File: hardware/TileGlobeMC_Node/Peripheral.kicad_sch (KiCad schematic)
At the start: 0 parts

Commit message: PCB progress
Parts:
- added C27: 4.7u, Capacitor_SMD:C_0603_1608Metric, symbol Device:C_Small
- added C28, C29, C30, C31, C32, C33, C34, C35: 100n, Capacitor_SMD:C_0603_1608Metric, symbol Device:C_Small
- added D3: 3V, Diode_SMD:D_SOD-323_HandSoldering, symbol Device:D_Zener_Small
- added J10: LCD, Connector_FFC-FPC:TE_1-1734839-2_1x12-1MP_P0.5mm_Horizontal, symbol Connector_Generic_MountingPin:Conn_01x12_MountingPin
- added JP3: BL_P1_1, Jumper:SolderJumper-2_P1.3mm_Open_TrianglePad1.0x1.5mm, symbol Jumper:SolderJumper_2_Open
- added JP4: BL_P1_2, Jumper:SolderJumper-2_P1.3mm_Open_TrianglePad1.0x1.5mm, symbol Jumper:SolderJumper_2_Open
- added JP5: BL_P1_3, Jumper:SolderJumper-2_P1.3mm_Open_TrianglePad1.0x1.5mm, symbol Jumper:SolderJumper_2_Open
- added R31, R42, R43, R44, R45, R46, R47: 100k, Capacitor_SMD:C_0603_1608Metric, symbol Device:R_Small
- added R35, R38, R39, R40, R41: 10k, Capacitor_SMD:C_0603_1608Metric, symbol Device:R_Small
- added SW1, SW2, SW3, SW4, SW5: Left, Button_Switch_SMD:SW_SPST_PTS647_Sx38, symbol Switch:SW_Push
- added U8: LSM6DS3, Package_LGA:LGA-14_3x2.5mm_P0.5mm_LayoutBorder3x4y, symbol Sensor_Motion:LSM6DS3
- added U9: AW9523B, Package_DFN_QFN:QFN-24-1EP_4x4mm_P0.5mm_EP2.7x2.7mm, symbol Interface_Expansion:AW9523B
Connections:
- new net: R38.1, SW2.1
- new net: R41.1, SW5.1
- new net: R39.1, SW3.1
- new net: JP3.1 (A), U9.2 (P1_1)
- new net: R40.1, SW4.1
- new net: JP4.1 (A), U9.3 (P1_2)
- new net: JP5.1 (A), U9.4 (P1_3)
- new net +3V3: C27.1, C28.1, C29.1, C35.1, J10.3 (Pin_3), J10.4 (Pin_4), R46.1, R47.1, SW2.2, SW3.2, SW4.2, SW5.2, U8.12 (CS), U8.5 (VDDIO), U8.8 (VDD), U9.18 (AD0), U9.21 (VCC), U9.23 (~{RST})
- new net BTN_BOTTOM: C32.1, R39.2, R42.1, U9.11 (P0_5)
- new net BTN_CENTER: C30.1, D3.1 (K), R35.2, R45.1
- new net BTN_CENTER_VBUS: R35.1, SW1.1
- new net BTN_LEFT: C31.1, R31.1, R38.2, U9.10 (P0_4)
- new net BTN_RIGHT: C33.1, R40.2, R43.1, U9.12 (P0_6)
- new net BTN_TOP: C34.1, R41.2, R44.1, U9.13 (P0_7)
- new net GND_PERI: C27.2, C28.2, C29.2, C30.2, C31.2, C32.2, C33.2, C34.2, C35.2, D3.2 (A), J10.1 (Pin_1), J10.12 (Pin_12), J10.5 (Pin_5), J10.6 (Pin_6), J10.MP (MountPin), R31.2, R42.2, R43.2, R44.2, R45.2, U8.1 (SDO/SA0), U8.2 (SDX), U8.3 (SCX), U8.6 (GND), U8.7 (GND), U9.24 (AD1), U9.25 (GND), U9.9 (GND)
- new net I2C_SCL: U8.13 (SCL), U9.19 (SCL)
- new net I2C_SDA: U8.14 (SDA), U9.20 (SDA)
- new net IMU_INT1: R46.2, U8.4 (INT1), U9.5 (P0_0)
- new net IMU_INT2: R47.2, U8.9 (INT2), U9.6 (P0_1)
- new net LCD_BL: J10.2 (Pin_2), JP3.2 (B), JP4.2 (B), JP5.2 (B), U9.1 (P1_0)
- new net LCD_CS: J10.8 (Pin_8)
- new net LCD_DC: J10.7 (Pin_7)
- new net LCD_MOSI: J10.10 (Pin_10)
- new net LCD_RST: J10.11 (Pin_11), U9.17 (P1_7)
- new net LCD_SCK: J10.9 (Pin_9)
- new net PERI_INT: U9.22 (~{INT})
- new net VBUS: SW1.2
- no-connect marks 0 -> 5
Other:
- note added: "Buttons"
- note added: "I2C Addr: 0x59"
- note added: "I2C Addr: 0x6A"
- note added: "I2C IO Expander & LCD BL Driver"
- note added: "IMU"
- note added: "LCD"

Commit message: PCB progress
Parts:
- added H5, H6, H7, H8: MountingHole, MountingHole:MountingHole_2.2mm_M2, symbol Mechanical:MountingHole
- added J11: USB_C, Connector_USB:USB_C_Receptacle_GCT_USB4105-xx-A_16P_TopMnt_Horizontal, symbol Connector:USB_C_Receptacle_USB2.0_16P
- added R32, R33: 5.1k, Resistor_SMD:R_0603_1608Metric, symbol Device:R_Small
- added R36, R37: 10k, Resistor_SMD:R_0603_1608Metric, symbol Device:R_Small
- D3: footprint Diode_SMD:D_SOD-323_HandSoldering -> Diode_SMD:D_SOD-523
- R31, R35, R38, R39, R40, R41, R42, R43, R44, R45, R46, R47: footprint Capacitor_SMD:C_0603_1608Metric -> Resistor_SMD:R_0603_1608Metric
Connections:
- net +3V3: now also R36.2, R37.2
- net GND_PERI: now also J11.A1 (GND), J11.A12 (GND), J11.B1 (GND), J11.B12 (GND), J11.S1 (SHIELD), R32.1, R33.1
- net I2C_SCL: now also R36.1
- net I2C_SDA: now also R37.1
- new net: J11.A5 (CC1), R33.2
- new net: J11.B5 (CC2), R32.2
- new net USB_D+: J11.A6 (D+), J11.B6 (D+)
- new net USB_D-: J11.A7 (D-), J11.B7 (D-)
- new net VIN: J11.A4 (VBUS), J11.A9 (VBUS), J11.B4 (VBUS), J11.B9 (VBUS)
- no-connect marks 5 -> 7
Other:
- note added: "USB-C"

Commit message: PCB done
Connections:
- net +3V3: now also J10.10 (Pin_10), J10.9 (Pin_9); no longer J10.3 (Pin_3), J10.4 (Pin_4)
- net BTN_BOTTOM: now also U9.10 (P0_4); no longer U9.11 (P0_5)
- net BTN_LEFT: now also U9.12 (P0_6); no longer U9.10 (P0_4)
- net BTN_RIGHT: now also U9.11 (P0_5); no longer U9.12 (P0_6)
- net GND_PERI: now also J10.7 (Pin_7), J10.8 (Pin_8); no longer J10.5 (Pin_5), J10.6 (Pin_6)
- net IMU_INT1: now also U9.7 (P0_2); no longer U9.5 (P0_0)
- net IMU_INT2: now also U9.8 (P0_3); no longer U9.6 (P0_1)
- net LCD_BL: now also J10.11 (Pin_11); no longer J10.2 (Pin_2)
- net LCD_CS: now also J10.5 (Pin_5); no longer J10.8 (Pin_8)
- net LCD_DC: now also J10.6 (Pin_6); no longer J10.7 (Pin_7)
- net LCD_MOSI: now also J10.3 (Pin_3); no longer J10.10 (Pin_10)
- net LCD_RST: now also J10.2 (Pin_2), U9.14 (P1_4); no longer J10.11 (Pin_11), U9.17 (P1_7)
- net LCD_SCK: now also J10.4 (Pin_4); no longer J10.9 (Pin_9)
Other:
- moved on the sheet: J10
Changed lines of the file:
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@@
 	)
 	(no_connect
-		(at 143.51 134.62)
+		(at 143.51 129.54)
 	)
 	(no_connect
-		(at 143.51 132.08)
+		(at 143.51 127)
 	)
 	(no_connect
@@
 	)
 	(no_connect
-		(at 143.51 160.02)
+		(at 143.51 167.64)
 	)
 	(no_connect
@@
 			(table_cell ""
 				(exclude_from_sim no)
-				(at 167.64 146.05 0)
+				(at 162.56 146.05 0)
 				(size 8.89 2.54)
 				(margins 0.9525 0.9525 0.9525 0.9525)
@@
 			(table_cell "1"
 				(exclude_from_sim no)
-				(at 167.64 148.59 0)
+				(at 162.56 148.59 0)
 				(size 8.89 2.54)
 				(margins 0.9525 0.9525 0.9525 0.9525)
@@
 			(table_cell "1"
 				(exclude_from_sim no)
-				(at 167.64 151.13 0)
+				(at 162.56 151.13 0)
 				(size 8.89 2.54)
 				(margins 0.9525 0.9525 0.9525 0.9525)
@@
 			(table_cell "1"
 				(exclude_from_sim no)
-				(at 167.64 153.67 0)
+				(at 162.56 153.67 0)
 				(size 8.89 2.54)
 				(margins 0.9525 0.9525 0.9525 0.9525)
@@
 			(table_cell "1"
 				(exclude_from_sim no)
-				(at 167.64 156.21 0)
+				(at 162.56 156.21 0)
 				(size 8.89 2.54)
 				(margins 0.9525 0.9525 0.9525 0.9525)
@@
 			(table_cell "0"
 				(exclude_from_sim no)
-				(at 167.64 158.75 0)
+				(at 162.56 158.75 0)
 				(size 8.89 2.54)
 				(margins 0.9525 0.9525 0.9525 0.9525)
@@
 			(table_cell "0"
 				(exclude_from_sim no)
-				(at 167.64 161.29 0)
+				(at 162.56 161.29 0)
 				(size 8.89 2.54)
 				(margins 0.9525 0.9525 0.9525 0.9525)
@@
 			(table_cell "0"
 				(exclude_from_sim no)
-				(at 167.64 163.83 0)
+				(at 162.56 163.83 0)
 				(size 8.89 2.54)
 				(margins 0.9525 0.9525 0.9525 0.9525)
@@
 			(table_cell "0"
 				(exclude_from_sim no)
-				(at 167.64 166.37 0)
+				(at 162.56 166.37 0)
 				(size 8.89 2.54)
 				(margins 0.9525 0.9525 0.9525 0.9525)
@@
 			(table_cell "Default"
 				(exclude_from_sim no)
-				(at 167.64 123.19 0)
+				(at 162.56 123.19 0)
 				(size 8.89 2.54)
 				(margins 0.9525 0.9525 0.9525 0.9525)
@@
 			(table_cell "Hi-Z"
 				(exclude_from_sim no)
-				(at 167.64 125.73 0)
+				(at 162.56 125.73 0)
 				(size 8.89 2.54)
 				(margins 0.9525 0.9525 0.9525 0.9525)
@@
 			(table_cell "Hi-Z"
 				(exclude_from_sim no)
-				(at 167.64 128.27 0)
+				(at 162.56 128.27 0)
 				(size 8.89 2.54)
 				(margins 0.9525 0.9525 0.9525 0.9525)
@@
 			(table_cell "Hi-Z"
 				(exclude_from_sim no)
-				(at 167.64 130.81 0)
+				(at 162.56 130.81 0)
 				(size 8.89 2.54)
 				(margins 0.9525 0.9525 0.9525 0.9525)
@@
 			(table_cell "Hi-Z"
 				(exclude_from_sim no)
-				(at 167.64 133.35 0)
+				(at 162.56 133.35 0)
 				(size 8.89 2.54)
 				(margins 0.9525 0.9525 0.9525 0.9525)
@@
 			(table_cell "0"
 				(exclude_from_sim no)
-				(at 167.64 135.89 0)
+				(at 162.56 135.89 0)
 				(size 8.89 2.54)
 				(margins 0.9525 0.9525 0.9525 0.9525)
@@
 			(table_cell "0"
 				(exclude_from_sim no)
-				(at 167.64 138.43 0)
+				(at 162.56 138.43 0)
 				(size 8.89 2.54)
 				(margins 0.9525 0.9525 0.9525 0.9525)
@@
 			(table_cell "0"
 				(exclude_from_sim no)
-				(at 167.64 140.97 0)
+				(at 162.56 140.97 0)
 				(size 8.89 2.54)
 				(margins 0.9525 0.9525 0.9525 0.9525)
@@
 			(table_cell "0"
 				(exclude_from_sim no)
-				(at 167.64 143.51 0)
+				(at 162.56 143.51 0)
 				(size 8.89 2.54)
 				(margins 0.9525 0.9525 0.9525 0.9525)
@@
 	(global_label "LCD_RST"
 		(shape output)
-		(at 143.51 167.64 0)
+		(at 143.51 160.02 0)
 		(fields_autoplaced yes)
 		(effects
@@
 		)
 		(property "Intersheetrefs" "${INTERSHEET_REFS}"
-			(at 154.478 167.64 0)
+			(at 154.478 160.02 0)
 			(effects
 				(font
@@
 	(global_label "BTN_LEFT"
 		(shape input)
-		(at 143.51 137.16 0)
+		(at 143.51 142.24 0)
 		(fields_autoplaced yes)
 		(effects
@@
 		)
 		(property "Intersheetrefs" "${INTERSHEET_REFS}"
-			(at 155.2642 137.16 0)
+			(at 155.2642 142.24 0)
 			(effects
 				(font
@@
 	(global_label "BTN_RIGHT"
 		(shape input)
-		(at 143.51 142.24 0)
+		(at 143.51 139.7 0)
 		(fields_autoplaced yes)
 		(effects
@@
 		)
 		(property "Intersheetrefs" "${INTERSHEET_REFS}"
-			(at 156.4738 142.24 0)
+			(at 156.4738 139.7 0)
 			(effects
 				(font
@@
 	(global_label "BTN_BOTTOM"
 		(shape input)
-		(at 143.51 139.7 0)
+		(at 143.51 137.16 0)
 		(fields_autoplaced yes)
 		(effects
@@
 		)
 		(property "Intersheetrefs" "${INTERSHEET_REFS}"
-			(at 158.3485 139.7 0)
+			(at 158.3485 137.16 0)
 			(effects
 				(font
@@
 	(global_label "IMU_INT2"
 		(shape input)
-		(at 143.51 129.54 0)
+		(at 143.51 134.62 0)
 		(fields_autoplaced yes)
 		(effects
@@
 		)
 		(property "Intersheetrefs" "${INTERSHEET_REFS}"
-			(at 154.9619 129.54 0)
+			(at 154.9619 134.62 0)
 			(effects
 				(font
@@
 	(global_label "IMU_INT1"
 		(shape input)
-		(at 143.51 127 0)
+		(at 143.51 132.08 0)
 		(fields_autoplaced yes)
 		(effects
@@
 		)
 		(property "Intersheetrefs" "${INTERSHEET_REFS}"
-			(at 154.9619 127 0)
+			(at 154.9619 132.08 0)
 			(effects
 				(font
@@
 	(symbol
 		(lib_id "power:GND")
-		(at 154.94 66.04 0)
+		(at 154.94 27.94 90)
 		(unit 1)
 		(exclude_from_sim no)
@@
 		(dnp no)
 		(property "Reference" "#PWR063"
-			(at 154.94 72.39 0)
+			(at 161.29 27.94 0)
 			(effects
 				(font
@@
 		)
 		(property "Value" "GND_PERI"
-			(at 154.94 69.596 0)
+			(at 158.496 27.94 0)
 			(effects
 				(font
@@
 		)
 		(property "Footprint" ""
-			(at 154.94 66.04 0)
+			(at 154.94 27.94 0)
 			(effects
 				(font
@@
 		)
 		(property "Datasheet" ""
-			(at 154.94 66.04 0)
+			(at 154.94 27.94 0)
 			(effects
 				(font
@@
 		)
 		(property "Description" "Power symbol creates a global label with name \"GND\" , ground"
-			(at 154.94 66.04 0)
+			(at 154.94 27.94 0)
 			(effects
 				(font
@@
 	(symbol
 		(lib_id "Connector_Generic_MountingPin:Conn_01x12_MountingPin")
-		(at 154.94 45.72 0)
+		(at 154.94 48.26 0)
+		(mirror x)
 		(unit 1)
 		(exclude_from_sim no)
@@
 		(dnp no)
 		(property "Reference" "J10"
-			(at 164.084 45.974 0)
+			(at 164.084 48.006 0)
 			(effects
 				(font
@@
 		)
 		(property "Value" "LCD"
-			(at 164.084 48.514 0)
+			(at 164.084 45.466 0)
 			(effects
 				(font
@@
 		)
 		(property "Footprint" "Connector_FFC-FPC:TE_1-1734839-2_1x12-1MP_P0.5mm_Horizontal"
-			(at 154.94 45.72 0)
+			(at 154.94 48.26 0)
 			(effects
 				(font
@@
 		)
 		(property "Datasheet" "~"
-			(at 154.94 45.72 0)
+			(at 154.94 48.26 0)
 			(effects
 				(font
@@
 		)
 		(property "Description" "Generic connectable mounting pin connector, single row, 01x12, script generated (kicad-library-utils/schlib/autogen/connector/)"
-			(at 154.94 45.72 0)
+			(at 154.94 48.26 0)
 			(effects
 				(font

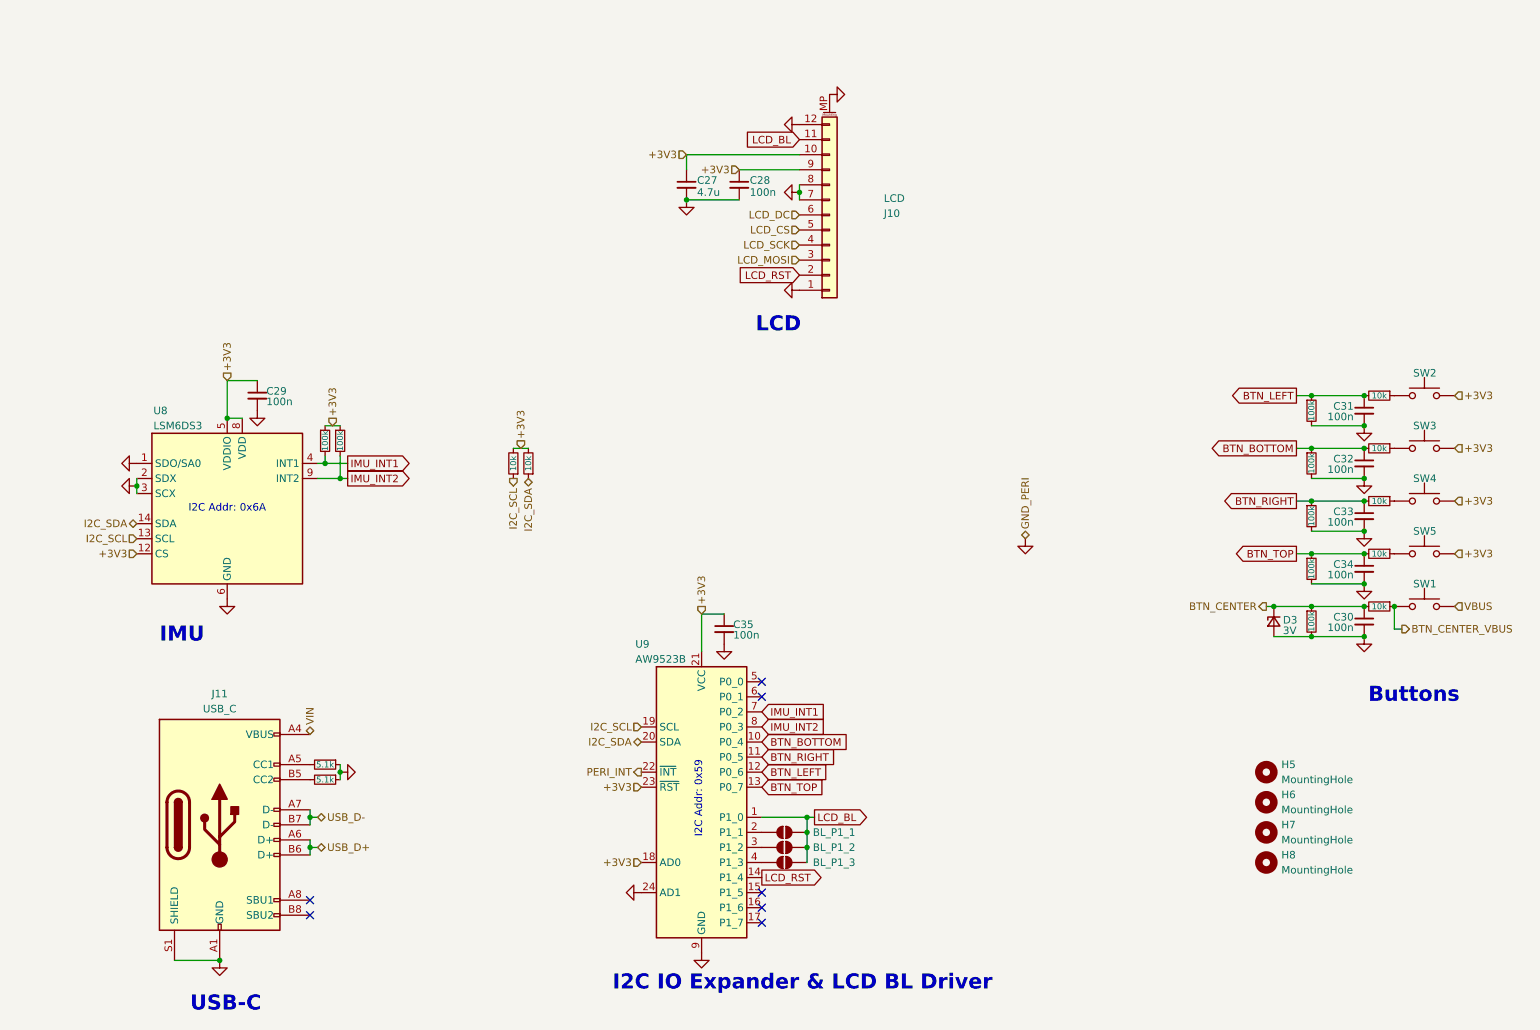
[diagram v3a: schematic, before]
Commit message: BOM; PCB minor tweaks
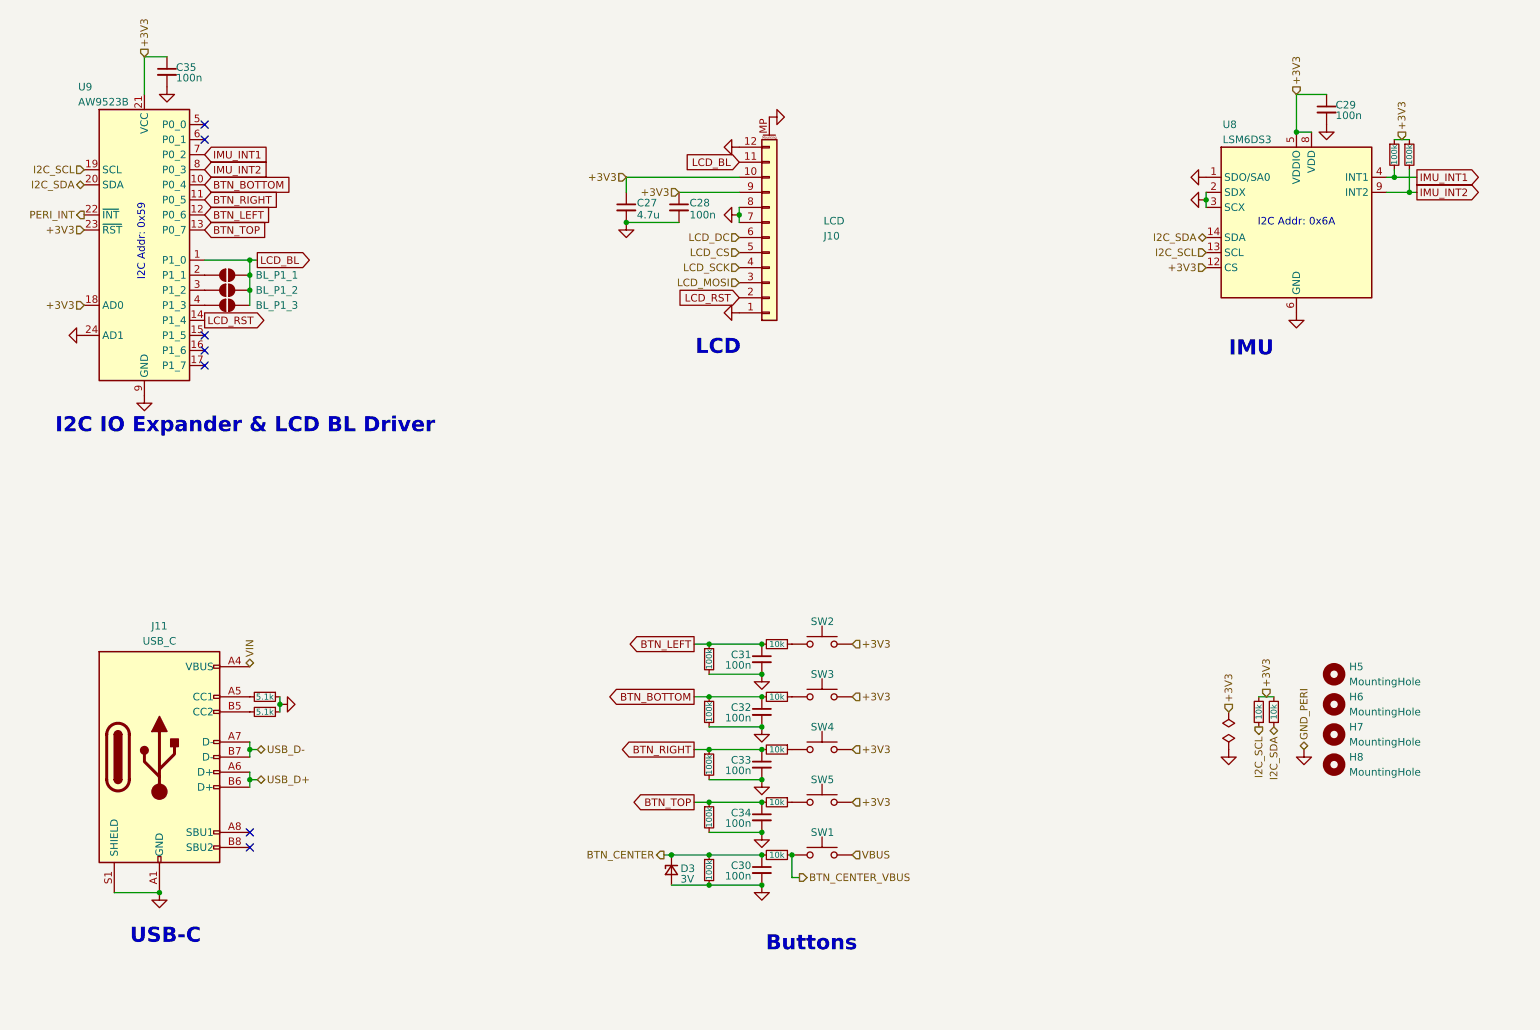
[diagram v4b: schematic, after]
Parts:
- C27: Link (none) -> https://www.lcsc.com/product-detail/C1705.html
- C28, C29, C30, C31, C32, C33, C34, C35: Link (none) -> https://www.lcsc.com/product-detail/C6119867.html
- D3: Link (none) -> https://www.lcsc.com/product-detail/C6771811.html
- H5, H6, H7, H8, JP3, JP4, JP5: now in the parts list
- J10: Link (none) -> https://www.lcsc.com/product-detail/C262559.html
- J11: Link (none) -> https://www.lcsc.com/product-detail/C2765186.html
- R31, R32, R33, R42, R43, R44, R45, R46, R47: Link (none) -> https://www.lcsc.com/product-detail/C2907002.html
- R35, R36, R37, R38, R39, R40, R41: Link (none) -> https://www.lcsc.com/product-detail/C2906982.html
- SW1: value Left -> Center
- SW3: value Left -> Bottom
- SW4: value Left -> Right
- SW5: value Left -> Top
- U8: Link (none) -> https://www.lcsc.com/product-detail/C967633.html?s_z=n_LSM6D
- U9: Link (none) -> https://www.lcsc.com/product-detail/C148077.html?s_z=n_AW95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
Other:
- moved on the sheet: C27, C28, C29, C30, C31, C32, C33, C34, C35, D3, H5, H6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
